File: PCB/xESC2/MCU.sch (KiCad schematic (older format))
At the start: 1 part, among them U4 STM32F405RGTx

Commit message: wip xESC2 logic
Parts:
- added C15: 100nF/100V, Capacitor_SMD:C_0805_2012Metric, symbol Device:C
- added Y1: Crystal, Crystal:Crystal_SMD_HC49-SD, symbol Device:Crystal
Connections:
- net labels added: +3.3V, GND
- wire segments 0 -> 19
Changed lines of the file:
@@
+	1    0    0    -1
+$EndComp
+Wire Wire Line
+	3250 5150 3250 5600
+Wire Wire Line
+	3250 5600 3350 5600
+Wire Wire Line
+	3450 5600 3450 5150
+Wire Wire Line
+	3350 5150 3350 5600
+Connection ~ 3350 5600
+Wire Wire Line
+	3350 5600 3450 5600
+Wire Wire Line
+	3350 5600 3350 5850
+$Comp
+L power:GND #PWR0123
+U 1 1 61A9A167
+P 3350 5850
+F 0 "#PWR0123" H 3350 5600 50  0001 C CNN
+F 1 "GND" H 3355 5677 50  0000 C CNN
+F 2 "" H 3350 5850 50  0001 C CNN
+F 3 "" H 3350 5850 50  0001 C CNN
+	1    3350 5850
+	1    0    0    -1
+$EndComp
+$Comp
+L Device:C C?
+U 1 1 61A9BC8B
+P 6550 3650
+AR Path="/61A3F4E8/61A9BC8B" Ref="C?"  Part="1"
+AR Path="/61AC26FB/61A9BC8B" Ref="C15"  Part="1"
+F 0 "C15" H 6665 3696 50  0000 L CNN
+F 1 "100nF/100V" H 6665 3605 50  0000 L CNN
+F 2 "Capacitor_SMD:C_0805_2012Metric" H 6588 3500 50  0001 C CNN
+F 3 "~" H 6550 3650 50  0001 C CNN
+	1    6550 3650
+	1    0    0    -1
+$EndComp
+$Comp
+L power:+3.3V #PWR?
+U 1 1 61A9F4B2
+P 3400 750
+AR Path="/61A9F4B2" Ref="#PWR?"  Part="1"
+AR Path="/61AC26FB/61A9F4B2" Ref="#PWR0124"  Part="1"
+F 0 "#PWR0124" H 3400 600 50  0001 C CNN
+F 1 "+3.3V" H 3415 923 50  0000 C CNN
+F 2 "" H 3400 750 50  0001 C CNN
+F 3 "" H 3400 750 50  0001 C CNN
+	1    3400 750
+	1    0    0    -1
+$EndComp
+Wire Wire Line
+	3400 750  3400 1150
+Wire Wire Line
+	3150 1550 3150 1150
+Wire Wire Line
+	3400 1150 3450 1150
+Wire Wire Line
+	3650 1150 3650 1550
+Connection ~ 3400 1150
+Wire Wire Line
+	3550 1550 3550 1150
+Connection ~ 3550 1150
+Wire Wire Line
+	3550 1150 3650 1150
+Wire Wire Line
+	3450 1500 3450 1150
+Connection ~ 3450 1150
+Wire Wire Line
+	3450 1150 3550 1150
+Wire Wire Line
+	3350 1550 3350 1150
+Connection ~ 3350 1150
+Wire Wire Line
+	3350 1150 3400 1150
+Wire Wire Line
+	3250 1550 3250 1150
+Wire Wire Line
+	3150 1150 3250 1150
+Connection ~ 3250 1150
+Wire Wire Line
+	3250 1150 3350 1150
+$Comp
+L Device:Crystal Y1
+U 1 1 61AA35C8
+P 5050 2950
+F 0 "Y1" H 5050 3218 50  0000 C CNN
+F 1 "Crystal" H 5050 3127 50  0000 C CNN
+F 2 "Crystal:Crystal_SMD_HC49-SD" H 5050 2950 50  0001 C CNN
+F 3 "~" H 5050 2950 50  0001 C CNN
+	1    5050 2950
 	1    0    0    -1
 $EndComp

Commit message: wip logic
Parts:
- removed C15: 100nF/100V, Capacitor_SMD:C_0805_2012Metric, symbol Device:C
- added C32, C33: 15pF, Capacitor_SMD:C_0603_1608Metric, symbol Device:C
- added C34, C37, C40, C41, C42, C43: 100nF/50V, Capacitor_SMD:C_0603_1608Metric, symbol Device:C
- added C35, C36, C38, C39: 2.2uF/50V, Capacitor_SMD:C_0805_2012Metric, symbol Device:C
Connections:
- net labels added: CAN_RX, CAN_TX, CUR_U, CUR_V, CUR_W, DRV_ENABLE, DRV_MISO, DRV_MOSI, DRV_NCS, DRV_SCK, FAULT, LED_GREEN, LED_RED, PCB_TEMP, PHASE_U, PHASE_V, PHASE_W, Reset, SERVO, SWDCLK, SWDIO, UH, UL, USB_DM, USDP_DP, VH, VL, WH, WL
- wire segments 19 -> 72
- no-connect marks 0 -> 9
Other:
- note added: "Place Near VDD Pins"
- note added: "Place near VDDA"
- moved on the sheet: Y1

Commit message: wip
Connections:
- net UH: now also U4.43 (PA10); no longer U4.41 (PA8)
- net WH: now also U4.41 (PA8); no longer U4.43 (PA10)
- net AN_IN: now reaches U4.11 (PC3)
- net SCK_EXT: now reaches U4.21 (PA5)
- net MISO_EXT: now reaches U4.22 (PA6)
- net TX_MOSI_EXT: now reaches U4.23 (PA7)
- net TX_MOSI_EXT: now also U4.29 (PB10)
- net TEMP_MOTOR: now reaches U4.24 (PC4)
- net RX_NCS_EXT: now reaches U4.30 (PB11)
- net HALL_3: now reaches U4.37 (PC6)
- net HALL_2: now reaches U4.38 (PC7)
- net HALL_1: now reaches U4.39 (PC8)
- no-connect marks 9 -> 11
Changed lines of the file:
@@
 	1200 3050 2650 3050
 NoConn ~ 2650 3250
-NoConn ~ 2650 3750
-NoConn ~ 2650 4250
 NoConn ~ 2650 4750
 NoConn ~ 4050 3650
@@
 NoConn ~ 2650 4950
 NoConn ~ 4050 3250
-Text HLabel 4050 2750 2    50   Output ~ 0
+Text HLabel 4050 2550 2    50   Output ~ 0
 WH
 Text HLabel 4050 2650 2    50   Output ~ 0
 VH
-Text HLabel 4050 2550 2    50   Output ~ 0
+Text HLabel 4050 2750 2    50   Output ~ 0
 UH
 Text HLabel 4050 4750 2    50   Output ~ 0
@@
 Text HLabel 2650 4450 0    50   Output ~ 0
 DRV_SCK
+Text HLabel 2650 3750 0    50   Input ~ 0
+AN_IN
+Text HLabel 2650 3850 0    50   Input ~ 0
+TEMP_MOTOR
+NoConn ~ 2650 3950
+Text HLabel 2650 4050 0    50   Input ~ 0
+HALL_3
+Text HLabel 2650 4150 0    50   Input ~ 0
+HALL_2
+Text HLabel 2650 4250 0    50   Input ~ 0
+HALL_1
+NoConn ~ 2650 4550
+NoConn ~ 2650 4650
+Text HLabel 4050 2250 2    50   Output ~ 0
+SCK_EXT
+Text HLabel 4050 2350 2    50   Input ~ 0
+MISO_EXT
+Text HLabel 4950 2450 2    50   Output ~ 0
+TX_MOSI_EXT
+Wire Wire Line
+	4950 2450 4700 2450
+Wire Wire Line
+	4050 4450 4700 4450
+Wire Wire Line
+	4700 4450 4700 2450
+Connection ~ 4700 2450
+Wire Wire Line
+	4700 2450 4050 2450
+Text HLabel 4050 4550 2    50   Input ~ 0
+RX_NCS_EXT
+NoConn ~ 4050 4650
 $EndSCHEMATC

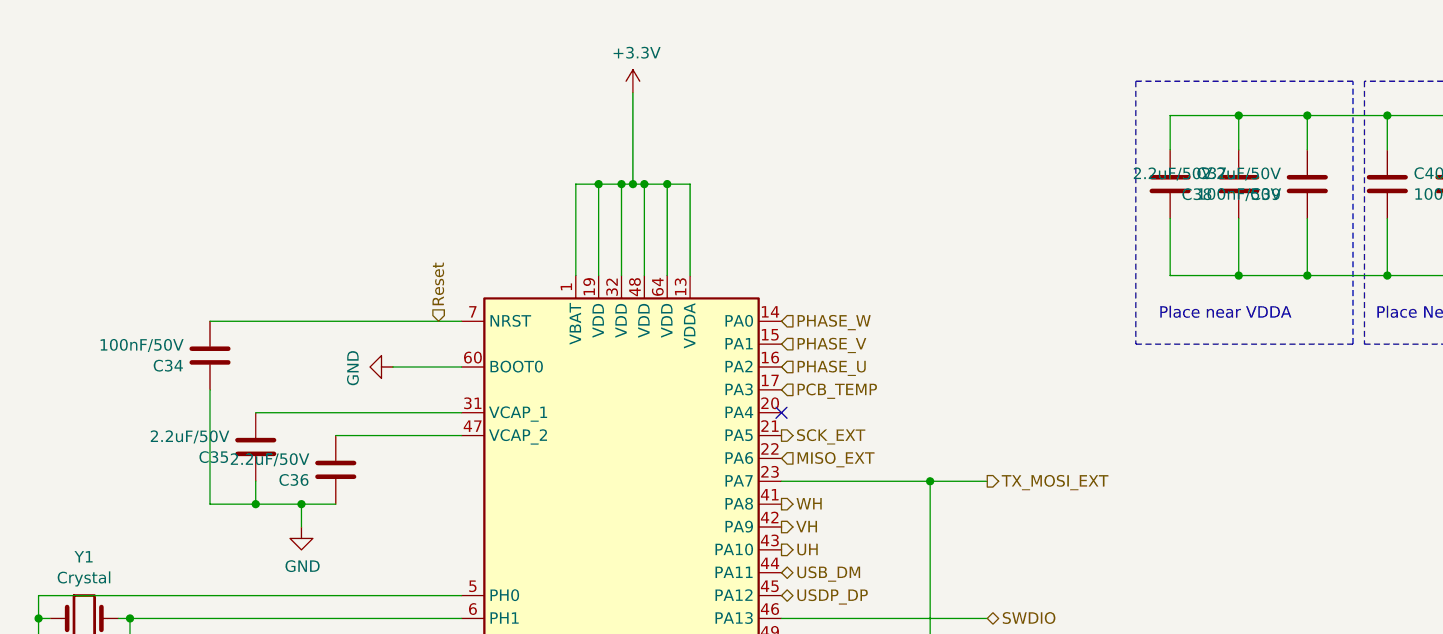
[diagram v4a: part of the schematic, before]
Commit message: changed some values, added BOM
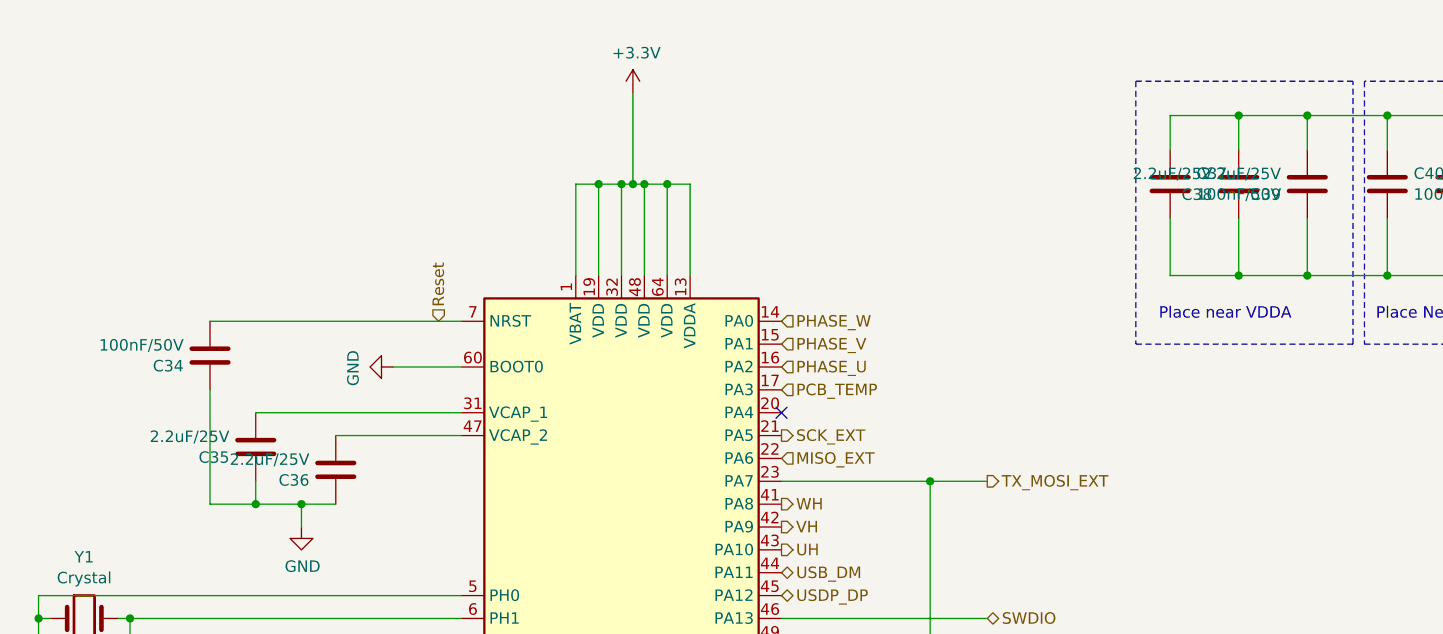
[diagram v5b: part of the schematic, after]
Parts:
- C35, C36, C38, C39: value 2.2uF/50V -> 2.2uF/25V
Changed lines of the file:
@@
 AR Path="/61AC26FB/61A6C9CC" Ref="C36"  Part="1"
 F 0 "C36" H 2215 2446 50  0000 L CNN
-F 1 "2.2uF/50V" H 2215 2355 50  0000 L CNN
+F 1 "2.2uF/25V" H 2215 2355 50  0000 L CNN
 F 2 "Capacitor_SMD:C_0805_2012Metric" H 2138 2250 50  0001 C CNN
 F 3 "~" H 2100 2400 50  0001 C CNN
@@
 AR Path="/61AC26FB/61A7737F" Ref="C35"  Part="1"
 F 0 "C35" H 1865 2346 50  0000 L CNN
-F 1 "2.2uF/50V" H 1865 2255 50  0000 L CNN
+F 1 "2.2uF/25V" H 1865 2255 50  0000 L CNN
 F 2 "Capacitor_SMD:C_0805_2012Metric" H 1788 2150 50  0001 C CNN
 F 3 "~" H 1750 2300 50  0001 C CNN
@@
 AR Path="/61AC26FB/61A7B997" Ref="C39"  Part="1"
 F 0 "C39" H 6465 1196 50  0000 L CNN
-F 1 "2.2uF/50V" H 6465 1105 50  0000 L CNN
+F 1 "2.2uF/25V" H 6465 1105 50  0000 L CNN
 F 2 "Capacitor_SMD:C_0805_2012Metric" H 6388 1000 50  0001 C CNN
 F 3 "~" H 6350 1150 50  0001 C CNN
@@
 AR Path="/61AC26FB/61A7C449" Ref="C38"  Part="1"
 F 0 "C38" H 6165 1196 50  0000 L CNN
-F 1 "2.2uF/50V" H 6165 1105 50  0000 L CNN
+F 1 "2.2uF/25V" H 6165 1105 50  0000 L CNN
 F 2 "Capacitor_SMD:C_0805_2012Metric" H 6088 1000 50  0001 C CNN
 F 3 "~" H 6050 1150 50  0001 C CNN
